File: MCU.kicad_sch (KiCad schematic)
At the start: 22 parts, among them J101 2.54mm 4-Pin JST, J201 Conn_01x04, SW201 SW_Push, U201 STM32F103C6Tx, Y201 8 MHz

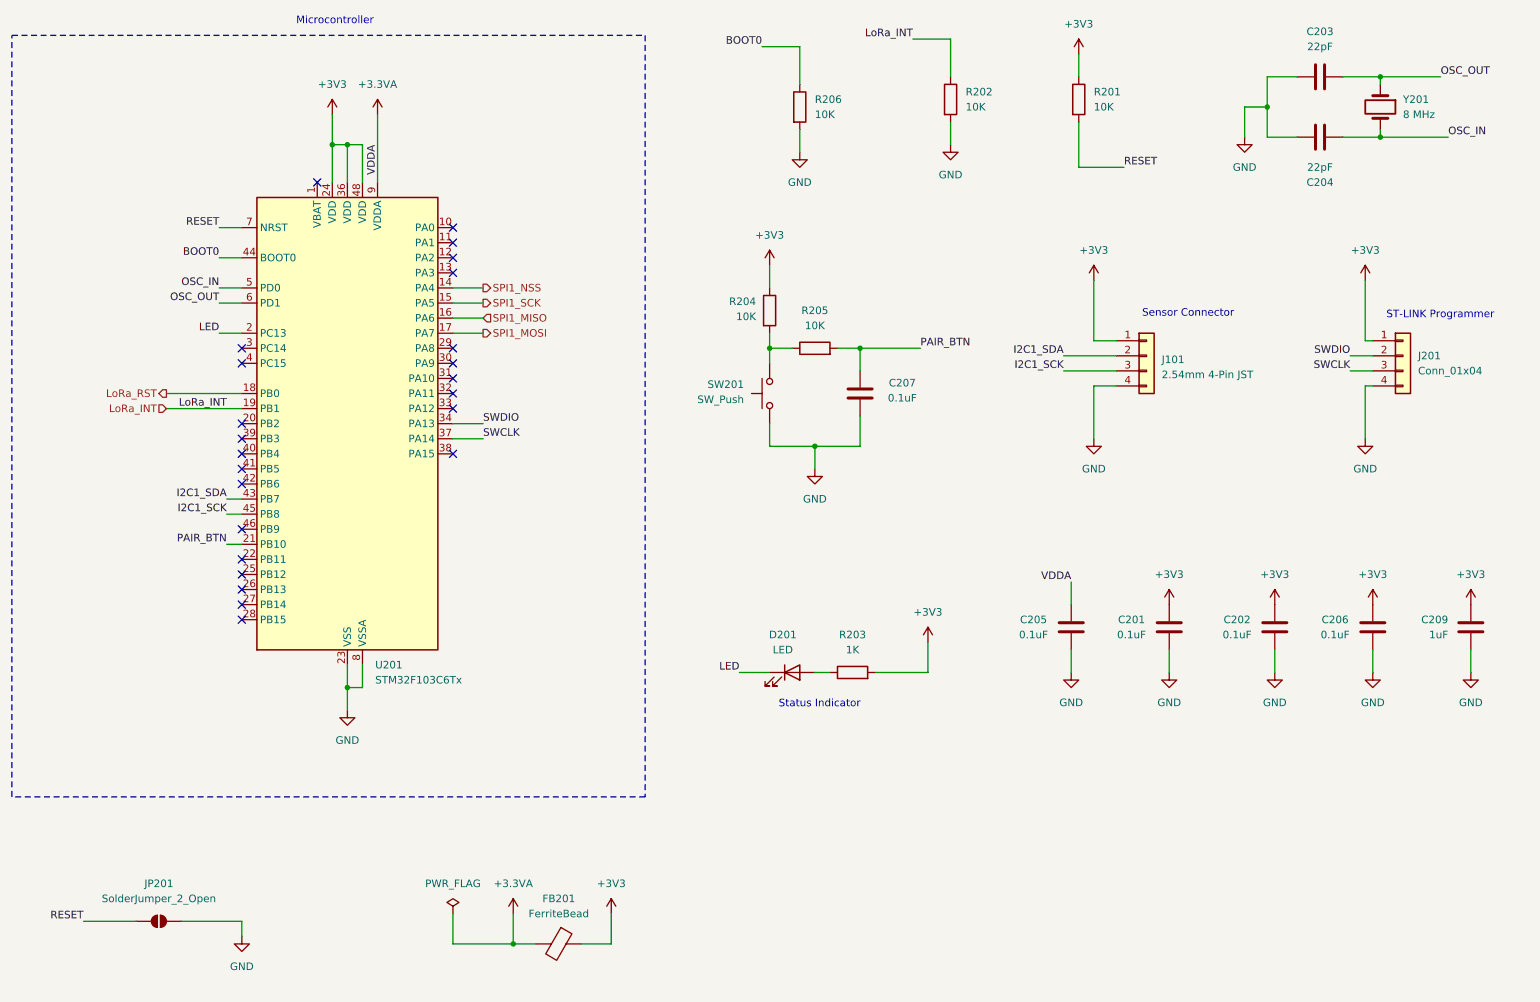
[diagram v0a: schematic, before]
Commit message: "Assign Footprints Done"
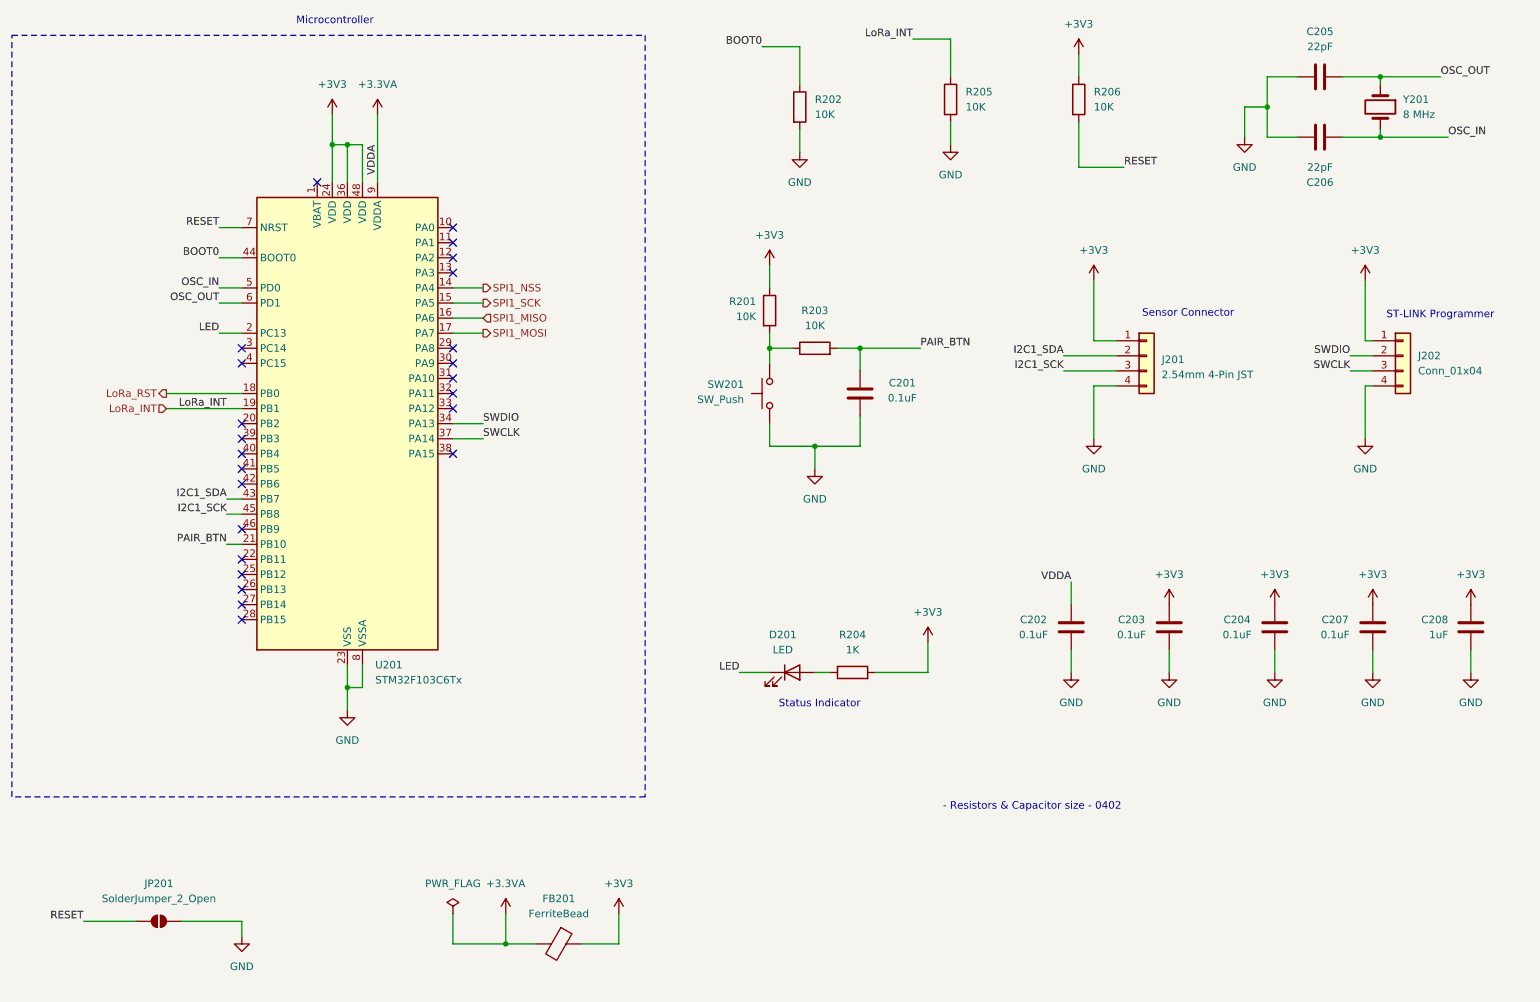
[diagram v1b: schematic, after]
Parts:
- C201: renamed from C207; footprint (none) -> Capacitor_SMD:C_0402_1005Metric_Pad0.74x0.62mm_HandSolder
- C202: renamed from C205; footprint (none) -> Capacitor_SMD:C_0402_1005Metric_Pad0.74x0.62mm_HandSolder
- C203: renamed from C201; footprint (none) -> Capacitor_SMD:C_0402_1005Metric_Pad0.74x0.62mm_HandSolder
- C204: renamed from C202; footprint (none) -> Capacitor_SMD:C_0402_1005Metric_Pad0.74x0.62mm_HandSolder
- C205: renamed from C203; footprint (none) -> Capacitor_SMD:C_0402_1005Metric_Pad0.74x0.62mm_HandSolder
- C206: renamed from C204; footprint (none) -> Capacitor_SMD:C_0402_1005Metric_Pad0.74x0.62mm_HandSolder
- C207: renamed from C206; footprint (none) -> Capacitor_SMD:C_0402_1005Metric_Pad0.74x0.62mm_HandSolder
- C208: renamed from C209; footprint (none) -> Capacitor_SMD:C_0402_1005Metric_Pad0.74x0.62mm_HandSolder
- D201: footprint (none) -> LED_THT:LED_D3.0mm
- FB201: footprint (none) -> Resistor_SMD:R_0402_1005Metric_Pad0.72x0.64mm_HandSolder
- J202: renamed from J201; footprint (none) -> Connector_PinHeader_2.54mm:PinHeader_1x04_P2.54mm_Vertical
- JP201: footprint (none) -> Jumper:SolderJumper-2_P1.3mm_Open_RoundedPad1.0x1.5mm
- R201: renamed from R204; footprint (none) -> Resistor_SMD:R_0402_1005Metric_Pad0.72x0.64mm_HandSolder
- R202: renamed from R206; footprint (none) -> Resistor_SMD:R_0402_1005Metric_Pad0.72x0.64mm_HandSolder
- R203: renamed from R205; footprint (none) -> Resistor_SMD:R_0402_1005Metric_Pad0.72x0.64mm_HandSolder
- R204: renamed from R203; footprint (none) -> Resistor_SMD:R_0402_1005Metric_Pad0.72x0.64mm_HandSolder
- R205: renamed from R202; footprint (none) -> Resistor_SMD:R_0402_1005Metric_Pad0.72x0.64mm_HandSolder
- R206: renamed from R201; footprint (none) -> Resistor_SMD:R_0402_1005Metric_Pad0.72x0.64mm_HandSolder
- SW201: footprint (none) -> Button_Switch_THT:SW_Tactile_SPST_Angled_PTS645Vx31-2LFS
- Y201: footprint (none) -> Crystal:Crystal_HC49-4H_Vertical
- renumbered J101 to J201
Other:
- note added: "- Resistors & Capacitor size - 0402"

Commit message: "I2c Pin change. PB6:SCL1 , PB7:SDA1"
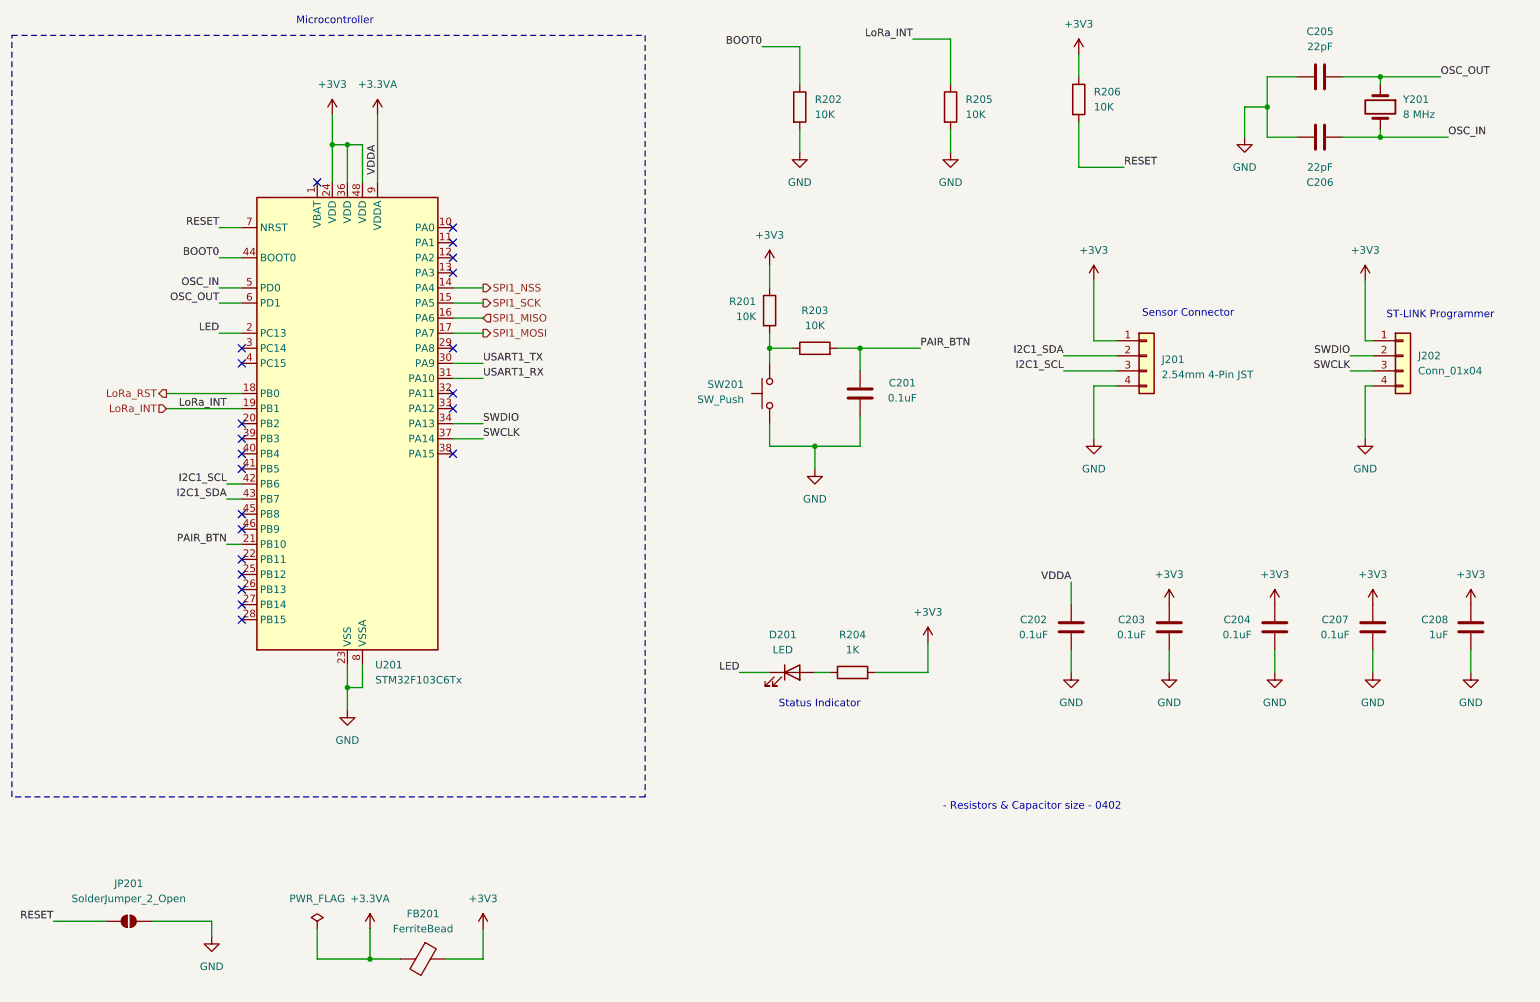
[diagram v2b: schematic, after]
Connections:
- net USART1_TX: now reaches U201.30 (PA9)
- net USART1_RX: now reaches U201.31 (PA10)
- net I2C1_SCL: now reaches U201.42 (PB6)
- net I2C1_SCL: now also J201.3 (Pin_3)
- net I2C1_SCK: no longer names the net of U201.45 (PB8)
- net I2C1_SCK: no longer J201.3 (Pin_3)
- no-connect marks 24 -> 22
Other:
- moved on the sheet: FB201, JP201, R205

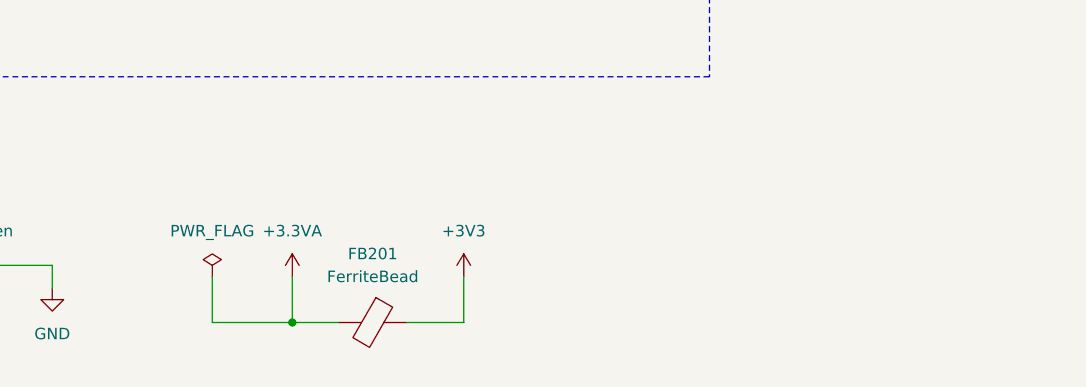
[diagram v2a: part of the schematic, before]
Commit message: "Debug port added in schematic"
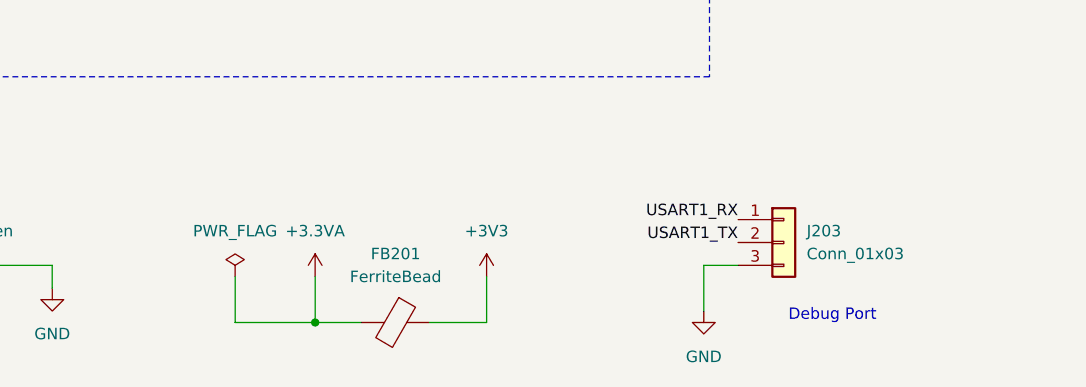
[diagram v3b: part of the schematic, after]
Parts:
- added J203: Conn_01x03, symbol Connector_Generic:Conn_01x03
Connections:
- net GND: now also J203.3 (Pin_3)
- net USART1_RX: now also J203.1 (Pin_1)
- net USART1_TX: now also J203.2 (Pin_2)
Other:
- note added: "Debug Port"
- moved on the sheet: FB201

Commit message: "PCB front Layer Component assembly done"
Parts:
- added R202, R206: 10K, Resistor_SMD:R_0402_1005Metric_Pad0.72x0.64mm_HandSolder, symbol Device:R
- J201: renamed from J203; footprint (none) -> Connector_PinHeader_2.54mm:PinHeader_1x03_P2.54mm_Vertical
- SW201: footprint Button_Switch_THT:SW_Tactile_SPST_Angled_PTS645Vx31-2LFS -> Connector_PinHeader_2.54mm:PinHeader_1x02_P2.54mm_Vertical
- renumbered J201 to J202, J202 to J203, R202 to R203, R203 to R204, R204 to R205, R205 to R207, R206 to R208
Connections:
- net +3V3: now also R202.1, R206.1
- net I2C1_SCL: now also R202.2
- net I2C1_SDA: now also R206.2
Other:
- moved on the sheet: D201, R205
